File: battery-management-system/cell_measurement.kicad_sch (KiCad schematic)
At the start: 21 parts, among them Q10 BS250FTA, Q11 BS250FTA, Q12 BS250FTA, Q13 BS250FTA, Q9 DMN3730U, U12 LM2904M8-13, U14 LM2904M8-13

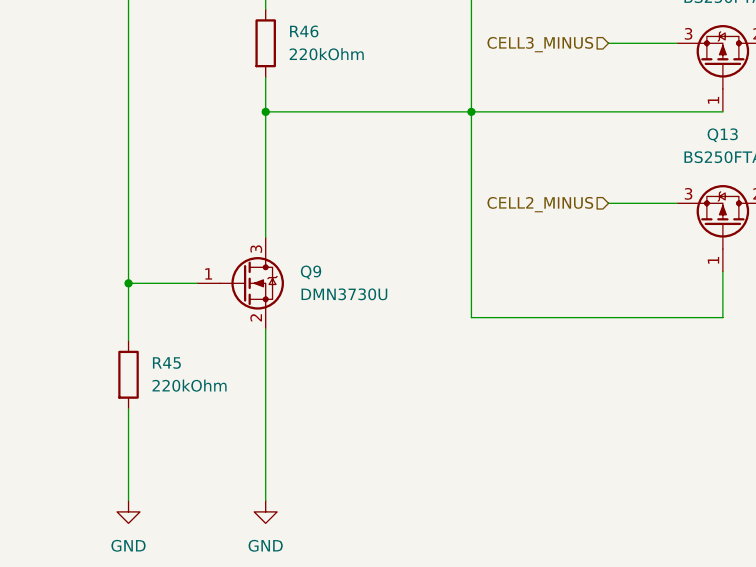
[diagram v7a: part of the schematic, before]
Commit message: switch to inductor based cell balancing
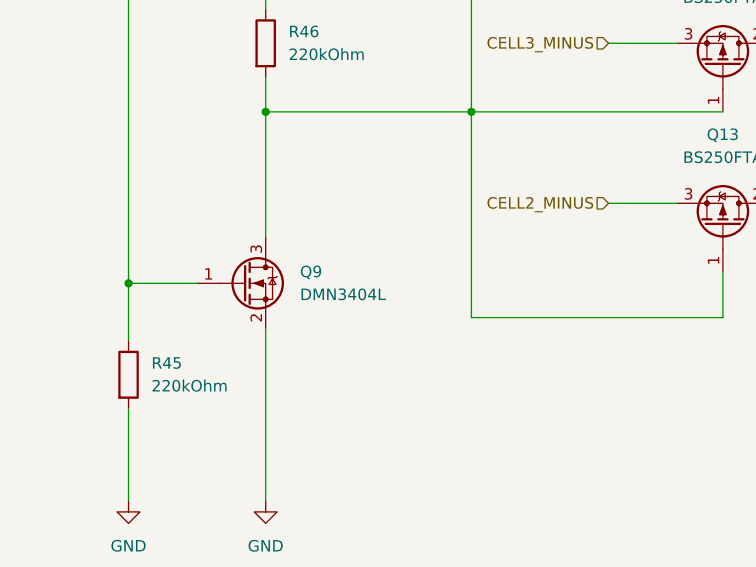
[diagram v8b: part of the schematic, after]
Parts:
- Q9: value DMN3730U -> DMN3404L; symbol benediktibk:DMN3730U -> benediktibk:DMN3404L; RS order number 823-2946 -> 751-4171
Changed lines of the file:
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@@
     )
   )
-  (symbol (lib_id "benediktibk:DMN3730U") (at 41.91 118.11 0) (unit 1)
+  (symbol (lib_id "benediktibk:DMN3404L") (at 41.91 118.11 0) (unit 1)
     (in_bom yes) (on_board yes) (dnp no) (fields_autoplaced)
-    (property "Reference" "Q9" (at 48.26 116.8399 0)
+    (property "Reference" "Q9" (at 48.26 116.84 0)
       (effects (font (size 1.27 1.27)) (justify left))
     )
-    (property "Value" "DMN3730U" (at 48.26 119.3799 0)
+    (property "Value" "DMN3404L" (at 48.26 119.38 0)
       (effects (font (size 1.27 1.27)) (justify left))
     )
@@
       (effects (font (size 1.27 1.27)) hide)
     )
-    (property "RS order number" "823-2946" (at 39.37 123.19 0)
+    (property "RS order number" "751-4171" (at 39.37 123.19 0)
       (effects (font (size 1.27 1.27)) hide)
     )
